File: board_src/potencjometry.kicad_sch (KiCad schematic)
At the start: 7 parts, among them J13 Conn_01x03, Q1 NPN, U2 MCP4431-xxxx-ST

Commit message: wersja dodane arkusze hierarchiczne
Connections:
- net 3,3V renamed +3.3V
- net gnd renamed GND
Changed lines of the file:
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@@
 	(wire
 		(pts
-			(xy 114.3 88.9) (xy 116.84 88.9)
+			(xy 114.3 88.9) (xy 119.38 88.9)
 		)
 		(stroke
@@
 			(width 0)
 			(type default)
-		)
-	)
-	(global_label "gnd"
-		(shape input)
-		(at 53.34 88.9 180)
-		(fields_autoplaced yes)
-		(effects
-			(font
-				(size 1.27 1.27)
-			)
-			(justify right)
-		)
-		(property "Intersheetrefs" "${INTERSHEET_REFS}"
-			(at 46.9078 88.9 0)
-			(effects
-				(font
-					(size 1.27 1.27)
-				)
-				(justify right)
-				(hide yes)
-			)
-		)
-	)
-	(global_label "3,3V"
-		(shape input)
-		(at 116.84 88.9 0)
-		(fields_autoplaced yes)
-		(effects
-			(font
-				(size 1.27 1.27)
-			)
-			(justify left)
-		)
-		(property "Intersheetrefs" "${INTERSHEET_REFS}"
-			(at 123.9376 88.9 0)
-			(effects
-				(font
-					(size 1.27 1.27)
-				)
-				(justify left)
-				(hide yes)
-			)
 		)
 	)
@@
 	)
 	(symbol
+		(lib_id "power:+3.3V")
+		(at 119.38 88.9 270)
+		(unit 1)
+		(exclude_from_sim no)
+		(in_bom yes)
+		(on_board yes)
+		(dnp no)
+		(fields_autoplaced yes)
+		(property "Reference" "#PWR013"
+			(at 115.57 88.9 0)
+			(effects
+				(font
+					(size 1.27 1.27)
+				)
+				(hide yes)
+			)
+		)
+		(property "Value" "+3.3V"
+			(at 123.19 88.8999 90)
+			(effects
+				(font
+					(size 1.27 1.27)
+				)
+				(justify left)
+			)
+		)
+		(property "Footprint" ""
+			(at 119.38 88.9 0)
+			(effects
+				(font
+					(size 1.27 1.27)
+				)
+				(hide yes)
+			)
+		)
+		(property "Datasheet" ""
+			(at 119.38 88.9 0)
+			(effects
+				(font
+					(size 1.27 1.27)
+				)
+				(hide yes)
+			)
+		)
+		(property "Description" "Power symbol creates a global label with name \"+3.3V\""
+			(at 119.38 88.9 0)
+			(effects
+				(font
+					(size 1.27 1.27)
+				)
+				(hide yes)
+			)
+		)
+		(pin "1"
+		)
+		(instances
+			(project "board"
+				(path "/772e9f49-cfcf-4cf6-843d-0684684f2d4b/6d56c433-3f02-4f8c-8dce-69e87751087b"
+					(reference "#PWR013")
+					(unit 1)
+				)
+			)
+		)
+	)
+	(symbol
 		(lib_id "Potentiometer_Digital:MCP4431-xxxx-ST")
 		(at 110.49 100.33 0)
@@
 					(unit 1)
 				)
+			)
+		)
+	)
+	(symbol
+		(lib_id "power:GND")
+		(at 53.34 88.9 270)
+		(unit 1)
+		(exclude_from_sim no)
+		(in_bom yes)
+		(on_board yes)
+		(dnp no)
+		(fields_autoplaced yes)
+		(property "Reference" "#PWR027"
+			(at 46.99 88.9 0)
+			(effects
+				(font
+					(size 1.27 1.27)
+				)
+				(hide yes)
+			)
+		)
+		(property "Value" "GND"
+			(at 49.53 88.8999 90)
+			(effects
+				(font
+					(size 1.27 1.27)
+				)
+				(justify right)
+			)
+		)
+		(property "Footprint" ""
+			(at 53.34 88.9 0)
+			(effects
+				(font
+					(size 1.27 1.27)
+				)
+				(hide yes)
+			)
+		)
+		(property "Datasheet" ""
+			(at 53.34 88.9 0)
+			(effects
+				(font
+					(size 1.27 1.27)
+				)
+				(hide yes)
+			)
+		)
+		(property "Description" "Power symbol creates a global label with name \"GND\" , ground"
+			(at 53.34 88.9 0)
+			(effects
+				(font
+					(size 1.27 1.27)
+				)
+				(hide yes)
+			)
+		)
+		(pin "1"
+		)
+		(instances
+			(project ""
+				(path "/772e9f49-cfcf-4cf6-843d-0684684f2d4b/6d56c433-3f02-4f8c-8dce-69e87751087b"
+					(reference "#PWR027")
+					(unit 1)
+				)

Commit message: wersja uzupelnione footprinty
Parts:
- J13: footprint (none) -> Connector_PinHeader_2.54mm:PinHeader_1x13_P2.54mm_Vertical
- LS1: footprint BMT0905XH05 -> footprints:BMT0905XH05
- Q1: footprint (none) -> Transistor_Power:GaN_Systems_GaNPX-3_5x6.6mm_Drain2.93x0.6mm
- R14, R2, R20: footprint (none) -> Resistor_SMD:R_0201_0603Metric
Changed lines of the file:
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@@
 			)
 		)
-		(property "Footprint" ""
+		(property "Footprint" "Connector_PinHeader_2.54mm:PinHeader_1x13_P2.54mm_Vertical"
 			(at 76.2 88.9 0)
 			(effects
@@
 			)
 		)
-		(property "Footprint" ""
+		(property "Footprint" "Resistor_SMD:R_0201_0603Metric"
 			(at 81.788 106.68 90)
 			(effects
@@
 			)
 		)
-		(property "Footprint" ""
+		(property "Footprint" "Resistor_SMD:R_0201_0603Metric"
 			(at 92.71 94.488 90)
 			(effects
@@
 			)
 		)
-		(property "Footprint" "BMT0905XH05"
+		(property "Footprint" "footprints:BMT0905XH05"
 			(at 124.46 218.11 0)
 			(effects
@@
 			)
 		)
-		(property "Footprint" ""
+		(property "Footprint" "Transistor_Power:GaN_Systems_GaNPX-3_5x6.6mm_Drain2.93x0.6mm"
 			(at 149.86 120.65 0)
 			(effects
@@
 			)
 		)
-		(property "Footprint" ""
+		(property "Footprint" "Resistor_SMD:R_0201_0603Metric"
 			(at 92.71 84.328 90)
 			(effects

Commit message: wersja 3d
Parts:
- removed U2: MCP4431-xxxx-ST, Package_SO:TSSOP-20_4.4x6.5mm_P0.65mm, symbol Potentiometer_Digital:MCP4431-xxxx-ST
- added VR1, VR2: PT6KV-251A2020, footprints:PT6KV251A2020, symbol PT6KV-251A2020:PT6KV-251A2020
- J13: footprint Connector_PinHeader_2.54mm:PinHeader_1x13_P2.54mm_Vertical -> Connector_PinHeader_2.54mm:PinHeader_1x03_P2.54mm_Vertical
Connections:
- net +3.3V: now also VR1.A1 (INITIAL), VR2.A1 (INITIAL)
- net GND: now also VR1.E1 (FINAL), VR2.E1 (FINAL)
- net at R14.2: now also VR2.S1 (WIPER)
- net at R2.2: now also VR1.S1 (WIPER)
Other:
- note removed: "jak podłączyć do magistrali?"

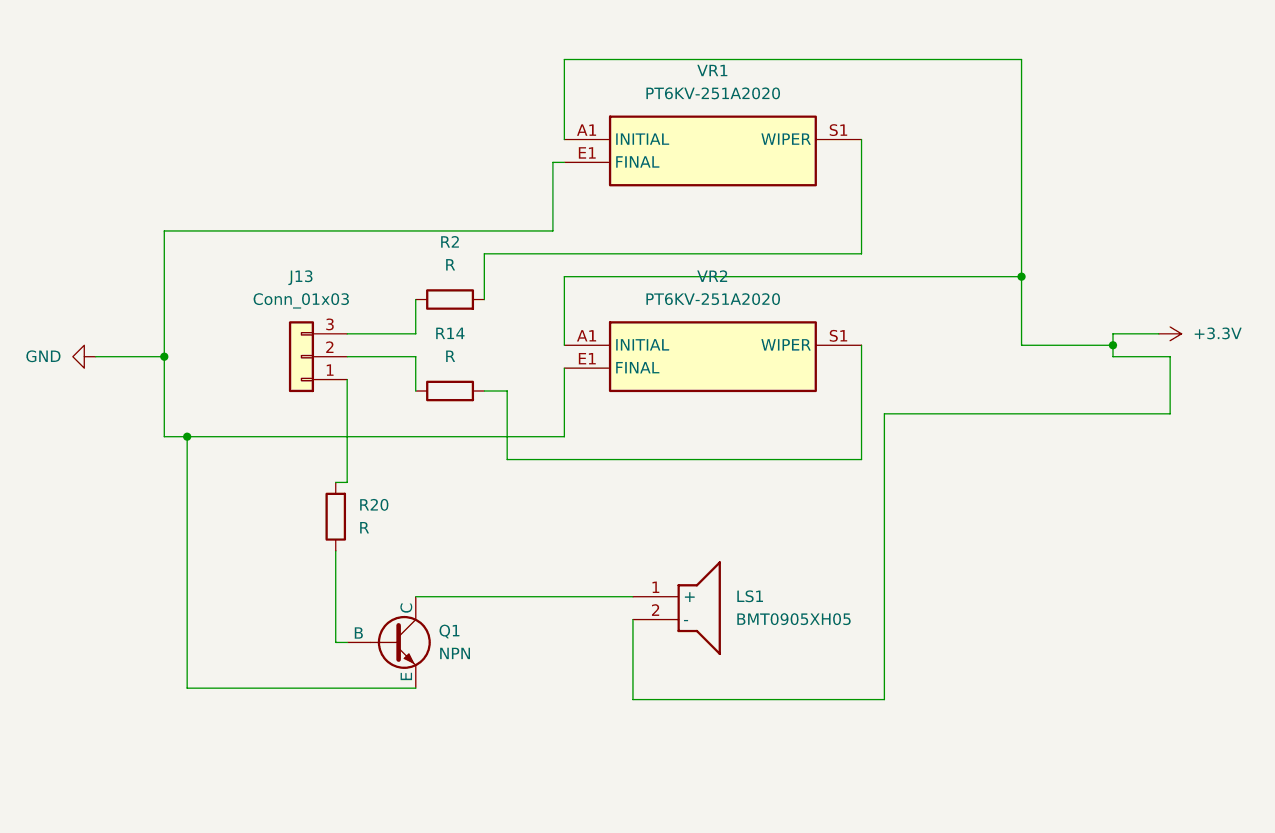
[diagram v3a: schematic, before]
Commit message: wersja z wyswietlaczem LCD
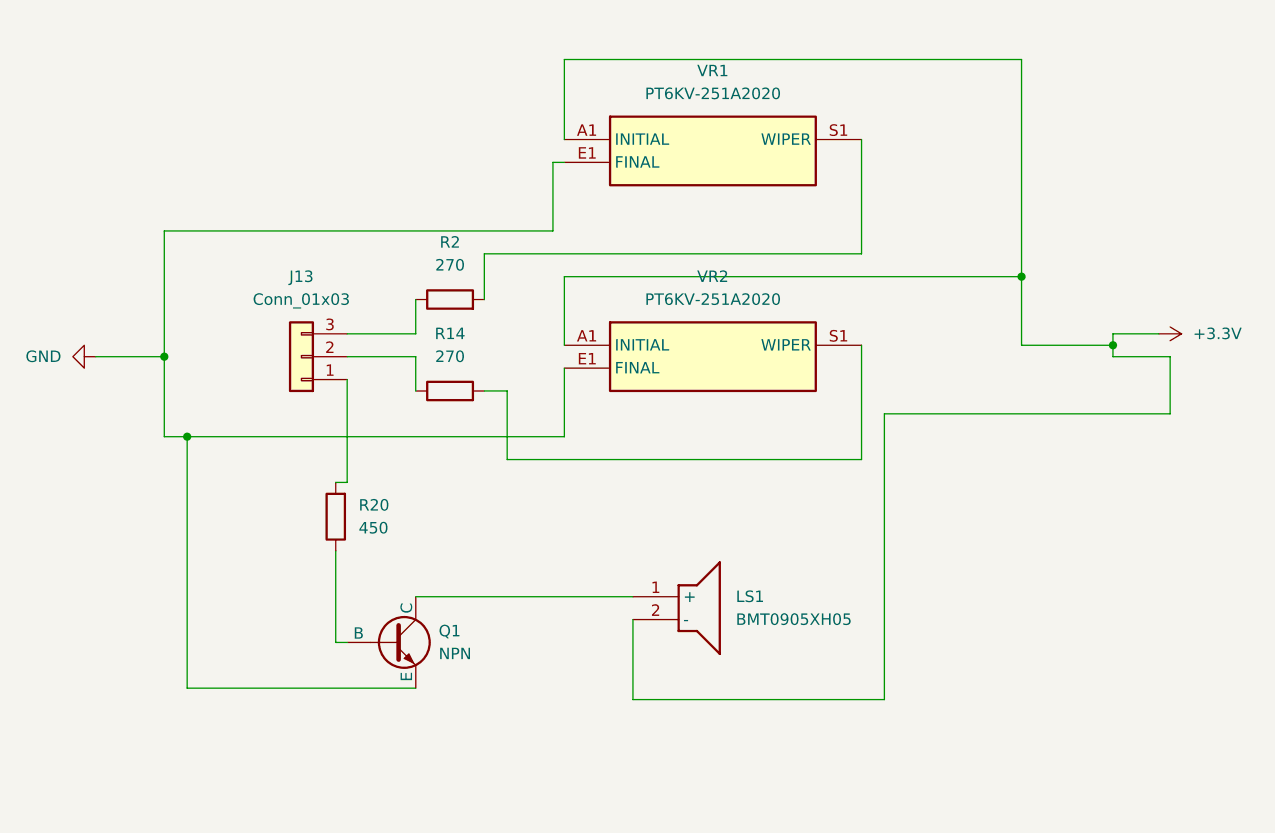
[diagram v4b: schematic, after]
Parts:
- Q1: footprint Transistor_Power:GaN_Systems_GaNPX-3_5x6.6mm_Drain2.93x0.6mm -> OptoDevice:Osram_SFH3710
- R14, R2: value R -> 270
- R20: value R -> 450
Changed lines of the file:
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@@
 			)
 		)
-		(property "Value" "R"
+		(property "Value" "450"
 			(at 82.55 107.9499 0)
 			(effects
@@
 			)
 		)
-		(property "Value" "R"
+		(property "Value" "270"
 			(at 92.71 88.9 90)
 			(effects
@@
 			)
 		)
-		(property "Footprint" "Transistor_Power:GaN_Systems_GaNPX-3_5x6.6mm_Drain2.93x0.6mm"
+		(property "Footprint" "OptoDevice:Osram_SFH3710"
 			(at 149.86 120.65 0)
 			(effects
@@
 			)
 		)
-		(property "Value" "R"
+		(property "Value" "270"
 			(at 92.71 78.74 90)
 			(effects

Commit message: wersja z FT232RN
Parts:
- R14, R2, R20: footprint Resistor_SMD:R_0201_0603Metric -> Resistor_SMD:R_1206_3216Metric
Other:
- note added: "zmienić symbol na zwykły"
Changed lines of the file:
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@@
 	(generator_version "9.0")
 	(paper "A4")
+	(text "zmienić symbol na zwykły\n"
+		(exclude_from_sim no)
+		(at 121.666 52.832 0)
+		(effects
+			(font
+				(size 1.27 1.27)
+			)
+		)
+	)
 	(junction
 		(at 63.5 97.79)
@@
 			)
 		)
-		(property "Footprint" "Resistor_SMD:R_0201_0603Metric"
+		(property "Footprint" "Resistor_SMD:R_1206_3216Metric"
 			(at 81.788 106.68 90)
 			(effects
@@
 			)
 		)
-		(property "Footprint" "Resistor_SMD:R_0201_0603Metric"
+		(property "Footprint" "Resistor_SMD:R_1206_3216Metric"
 			(at 92.71 94.488 90)
 			(effects
@@
 			)
 		)
-		(property "Footprint" "Resistor_SMD:R_0201_0603Metric"
+		(property "Footprint" "Resistor_SMD:R_1206_3216Metric"
 			(at 92.71 84.328 90)
 			(effects

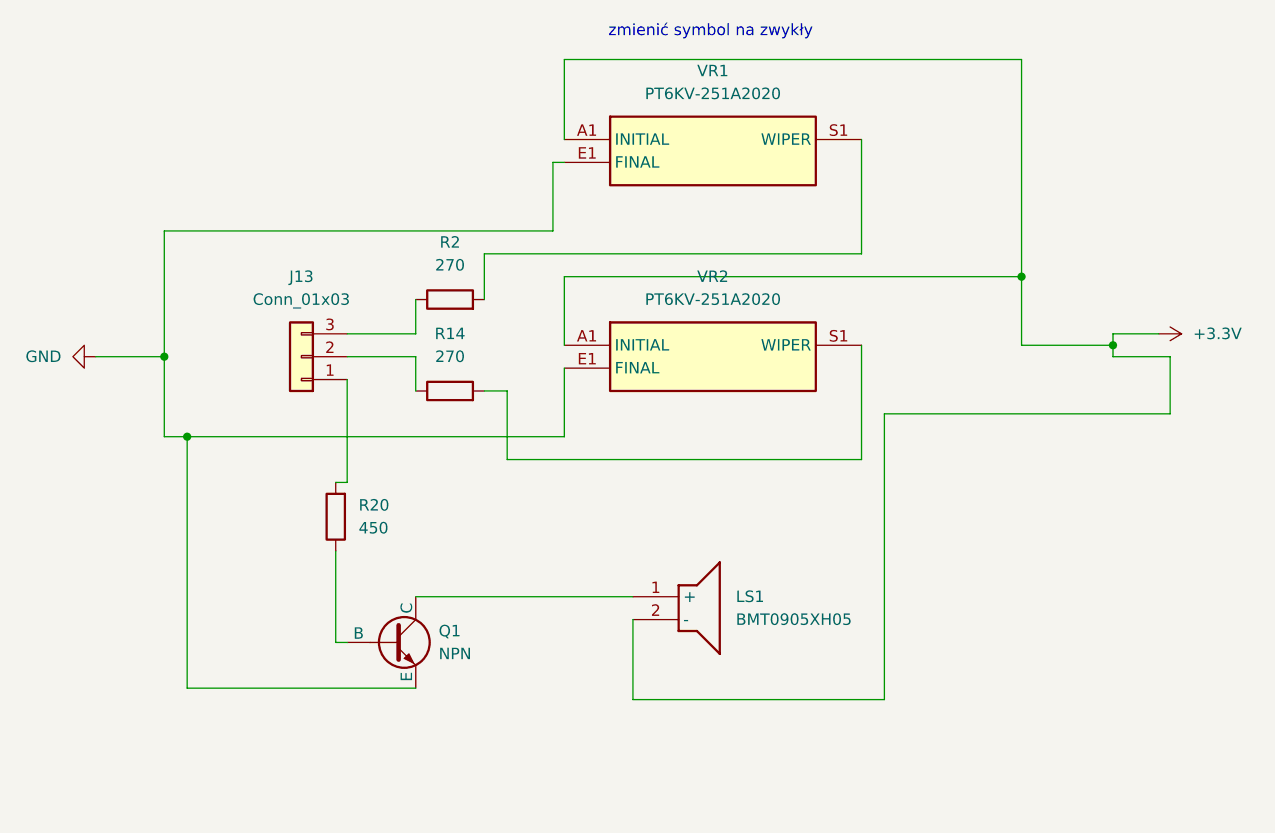
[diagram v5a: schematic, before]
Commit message: Wersja ze sciezkami miedzianymi
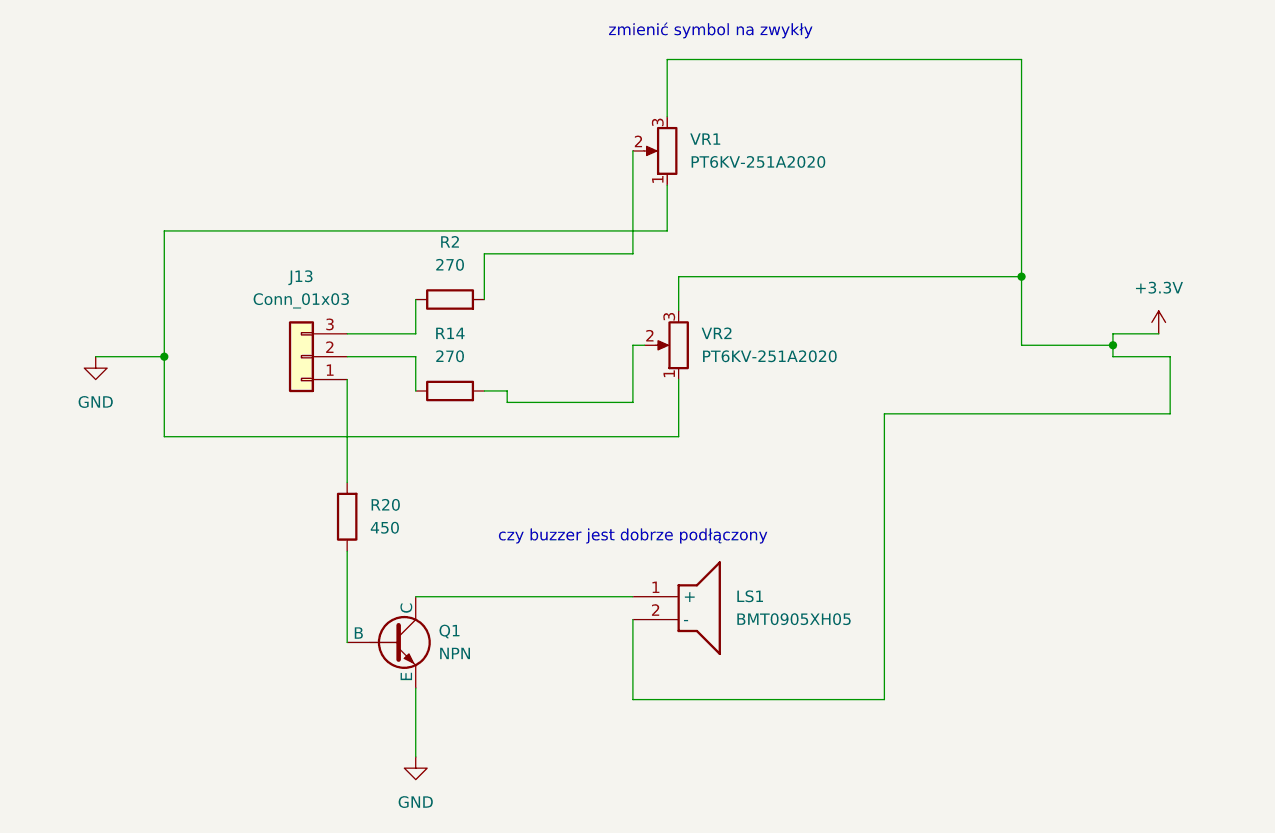
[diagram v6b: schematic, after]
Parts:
- Q1: footprint OptoDevice:Osram_SFH3710 -> Package_TO_SOT_SMD:SOT-23
- R14, R2, R20: footprint Resistor_SMD:R_1206_3216Metric -> Resistor_SMD:R_0603_1608Metric
- VR1, VR2: symbol PT6KV-251A2020:PT6KV-251A2020 -> Device:R_Potentiometer
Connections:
- net +3.3V: now also VR1.3, VR2.3; no longer VR1.A1 (INITIAL), VR2.A1 (INITIAL)
- net GND: now also VR1.1, VR2.1; no longer VR1.E1 (FINAL), VR2.E1 (FINAL)
- net at R14.2: now also VR2.2; no longer VR2.S1 (WIPER)
- net at R2.2: now also VR1.2; no longer VR1.S1 (WIPER)
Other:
- note added: "czy buzzer jest dobrze podłączony"
- moved on the sheet: R20

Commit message: sciezki polaczen
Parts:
- Q1: symbol Simulation_SPICE:NPN -> Transistor_BJT:SS8550
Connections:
- net GND: now also Q1.2 (E); no longer Q1.3 (E)
- net at R20.1: now also Q1.1 (B); no longer Q1.2 (B)
- net at LS1.1 (+): now also Q1.3 (C); no longer Q1.1 (C)
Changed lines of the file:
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@@
 	)
 	(symbol
-		(lib_id "Simulation_SPICE:NPN")
+		(lib_id "Transistor_BJT:SS8550")
 		(at 86.36 120.65 0)
 		(unit 1)
@@
 				)
 				(justify left)
+				(hide yes)
 			)
 		)
 		(property "Footprint" "Package_TO_SOT_SMD:SOT-23"
-			(at 149.86 120.65 0)
+			(at 91.44 128.016 0)
+			(effects
+				(font
+					(size 1.27 1.27)
+					(italic yes)
+				)
+				(justify left)
+				(hide yes)
+			)
+		)
+		(property "Datasheet" "http://www.secosgmbh.com/datasheet/products/SSMPTransistor/SOT-23/SS8550.pdf"
+			(at 91.44 125.476 0)
 			(effects
 				(font
 					(size 1.27 1.27)
 				)
+				(justify left)
 				(hide yes)
 			)
 		)
-		(property "Datasheet" "https://ngspice.sourceforge.io/docs/ngspice-html-manual/manual.xhtml#cha_BJTs"
-			(at 149.86 120.65 0)
+		(property "Description" "General Purpose PNP Transistor, 1.5A Ic, 25V Vce, SOT-23"
+			(at 120.396 122.936 0)
 			(effects
 				(font
-					(size 1.27 1.27)
-				)
-				(hide yes)
-			)
-		)
-		(property "Description" "Bipolar transistor symbol for simulation only, substrate tied to the emitter"
-			(at 86.36 120.65 0)
-			(effects
-				(font
